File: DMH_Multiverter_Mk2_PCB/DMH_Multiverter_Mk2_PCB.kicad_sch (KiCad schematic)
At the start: 0 parts

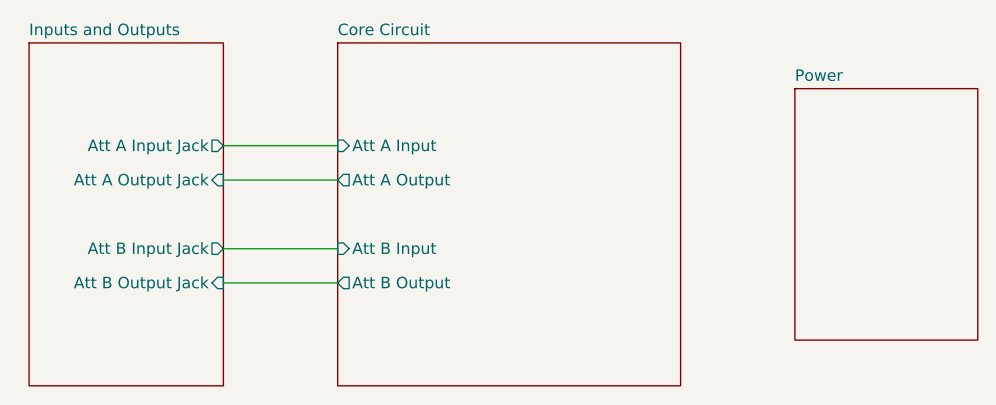
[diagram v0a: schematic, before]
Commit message: Added 3rd attenuverter to Panel and Schematic
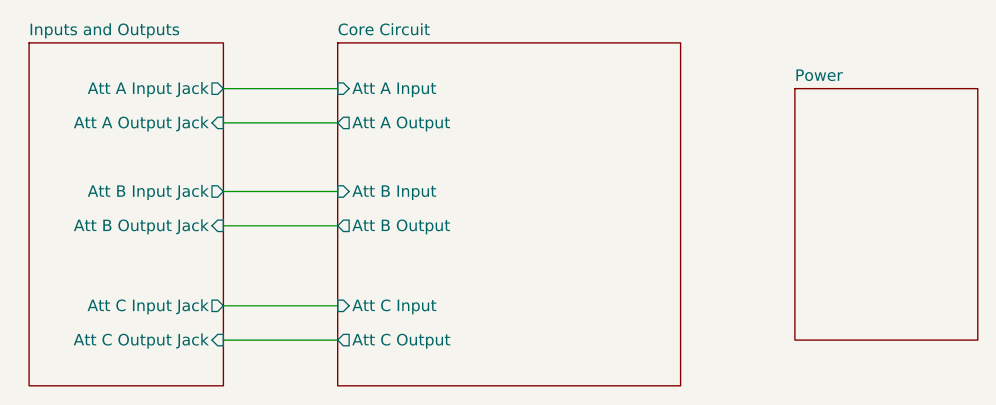
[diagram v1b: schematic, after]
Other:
- sheet Core Circuit ports: added Att C Input, Att C Output; removed none
- sheet Inputs and Outputs ports: added Att C Input Jack, Att C Output Jack; removed none
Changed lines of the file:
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@@
 	(wire
 		(pts
-			(xy 38.1 115.57) (xy 50.8 115.57)
-		)
-		(stroke
-			(width 0)
-			(type default)
-		)
-	)
-	(wire
-		(pts
-			(xy 38.1 111.76) (xy 50.8 111.76)
-		)
-		(stroke
-			(width 0)
-			(type default)
-		)
-	)
-	(wire
-		(pts
-			(xy 38.1 100.33) (xy 50.8 100.33)
-		)
-		(stroke
-			(width 0)
-			(type default)
-		)
-	)
-	(wire
-		(pts
-			(xy 38.1 104.14) (xy 50.8 104.14)
+			(xy 38.1 109.22) (xy 50.8 109.22)
+		)
+		(stroke
+			(width 0)
+			(type default)
+		)
+	)
+	(wire
+		(pts
+			(xy 38.1 105.41) (xy 50.8 105.41)
+		)
+		(stroke
+			(width 0)
+			(type default)
+		)
+	)
+	(wire
+		(pts
+			(xy 38.1 118.11) (xy 50.8 118.11)
+		)
+		(stroke
+			(width 0)
+			(type default)
+		)
+	)
+	(wire
+		(pts
+			(xy 38.1 121.92) (xy 50.8 121.92)
+		)
+		(stroke
+			(width 0)
+			(type default)
+		)
+	)
+	(wire
+		(pts
+			(xy 38.1 93.98) (xy 50.8 93.98)
+		)
+		(stroke
+			(width 0)
+			(type default)
+		)
+	)
+	(wire
+		(pts
+			(xy 38.1 97.79) (xy 50.8 97.79)
 		)
 		(stroke
@@
 		)
 		(instances
-			(project "DMH_Multiverter_PCB"
+			(project "DMH_Multiverter_Mk2_PCB"
 				(path "/58f4306d-5387-4983-bb08-41a2313fd315"
 					(page "4")
@@
 		)
 		(pin "Att B Output" output
-			(at 50.8 115.57 180)
+			(at 50.8 109.22 180)
 			(effects
 				(font
@@
 		)
 		(pin "Att A Output" output
-			(at 50.8 104.14 180)
+			(at 50.8 97.79 180)
 			(effects
 				(font
@@
 		)
 		(pin "Att A Input" input
-			(at 50.8 100.33 180)
+			(at 50.8 93.98 180)
 			(effects
 				(font
@@
 		)
 		(pin "Att B Input" input
-			(at 50.8 111.76 180)
+			(at 50.8 105.41 180)
+			(effects
+				(font
+					(size 1.27 1.27)
+				)
+				(justify left)
+			)
+		)
+		(pin "Att C Input" input
+			(at 50.8 118.11 180)
+			(effects
+				(font
+					(size 1.27 1.27)
+				)
+				(justify left)
+			)
+		)
+		(pin "Att C Output" output
+			(at 50.8 121.92 180)
 			(effects
 				(font
@@
 		)
 		(instances
-			(project "DMH_Multiverter_PCB"
+			(project "DMH_Multiverter_Mk2_PCB"
 				(path "/58f4306d-5387-4983-bb08-41a2313fd315"
 					(page "3")
@@
 		)
 		(pin "Att A Output Jack" input
-			(at 38.1 104.14 0)
+			(at 38.1 97.79 0)
 			(effects
 				(font
@@
 		)
 		(pin "Att B Input Jack" output
-			(at 38.1 111.76 0)
+			(at 38.1 105.41 0)
 			(effects
 				(font
@@
 		)
 		(pin "Att A Input Jack" output
-			(at 38.1 100.33 0)
+			(at 38.1 93.98 0)
 			(effects
 				(font
@@
 		)
 		(pin "Att B Output Jack" input
-			(at 38.1 115.57 0)
+			(at 38.1 109.22 0)
+			(effects
+				(font
+					(size 1.27 1.27)
+				)
+				(justify right)
+			)
+		)
+		(pin "Att C Input Jack" output
+			(at 38.1 118.11 0)
+			(effects
+				(font
+					(size 1.27 1.27)
+				)
+				(justify right)
+			)
+		)
+		(pin "Att C Output Jack" input
+			(at 38.1 121.92 0)
 			(effects
 				(font
@@
 		)
 		(instances
-			(project "DMH_Multiverter_PCB"
+			(project "DMH_Multiverter_Mk2_PCB"
 				(path "/58f4306d-5387-4983-bb08-41a2313fd315"
 					(page "2")
